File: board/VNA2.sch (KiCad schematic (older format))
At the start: 61 parts, among them U2 LM339, U3 SA612, U4 SA612, U5 SA612, U6 TL082, U7 TL082

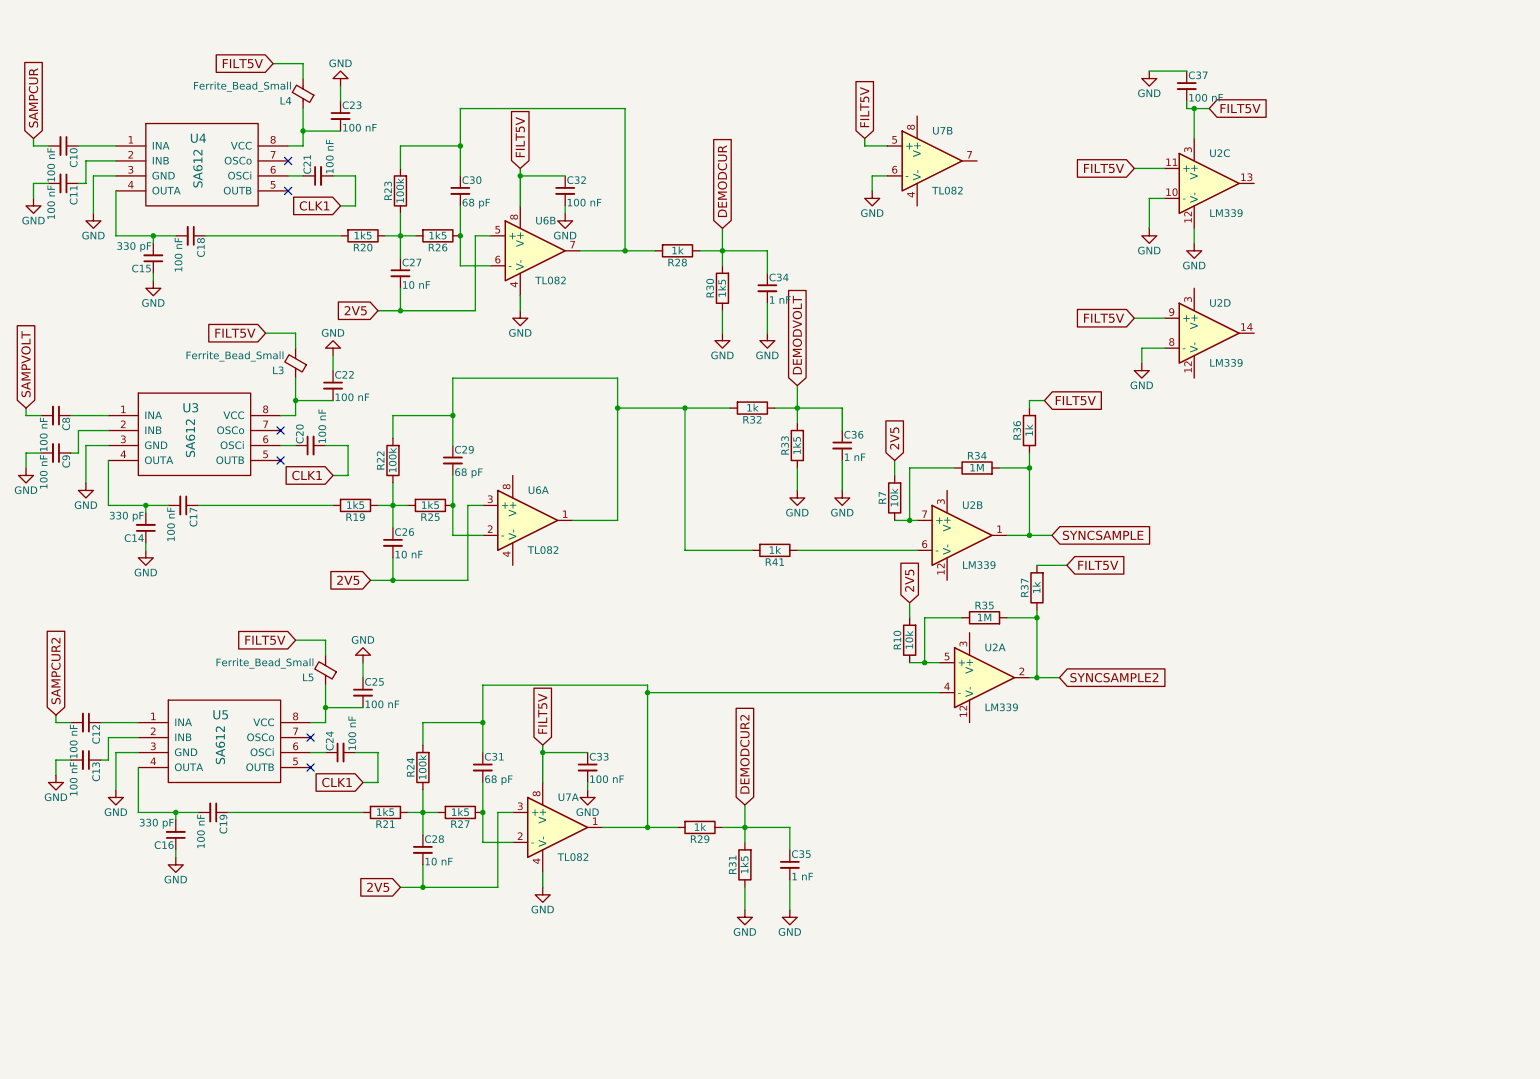
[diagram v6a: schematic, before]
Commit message: Changed TL082 to LM358, other corrections to software
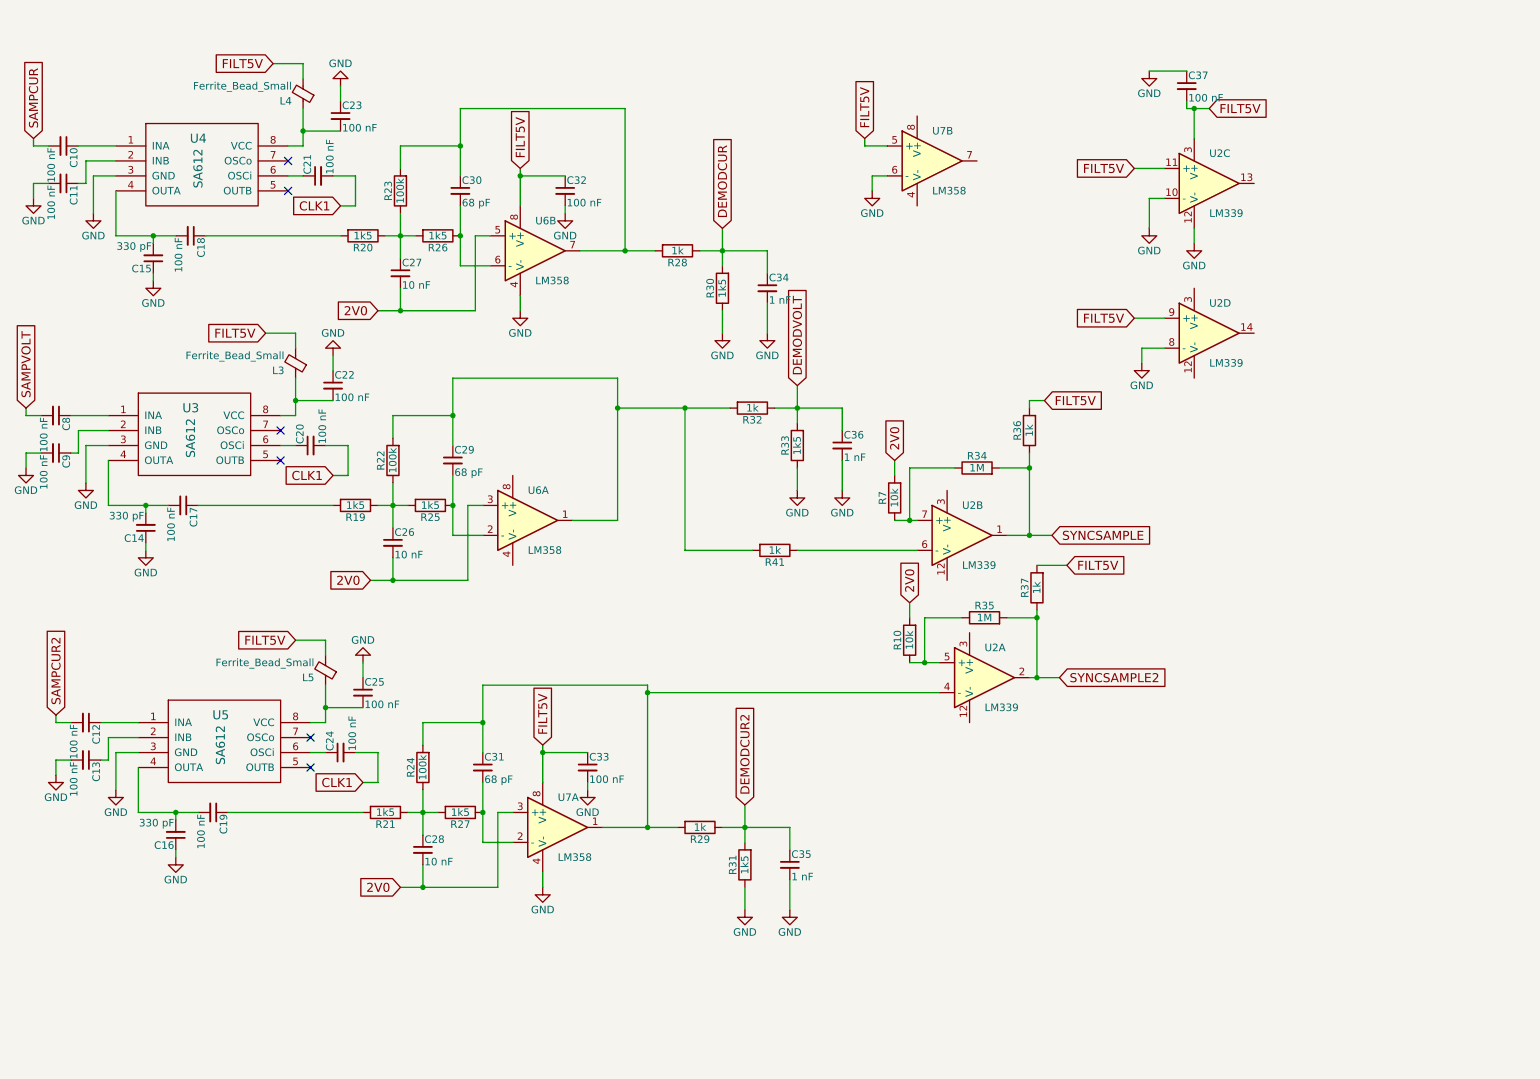
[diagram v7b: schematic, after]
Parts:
- removed U6, U7: TL082, Housings_DIP:DIP-8_W7.62mm_Socket, symbol TL082
- added U6, U7: LM358, Housings_DIP:DIP-8_W7.62mm_Socket, symbol LM358
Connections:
- net FILT5V: now also U6.8 (V+), U7.5 (+), U7.8 (V+)
- net GND: now also U6.4 (V-), U7.4 (V-), U7.6 (-)
- net at C30.2, R26.1: now also U6.6 (-)
- net at C30.1, R23.2, R28.2: now also U6.7
- net at C29.1, R22.2, R32.2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: now also U6.1
- net at C29.2, R25.1: now also U6.2 (-)
- net at C31.1, R24.2, R29.2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: now also U7.1
- net at C31.2, R27.1: now also U7.2 (-)
- net 2V5 renamed 2V0
- net 2V0: now also U6.3 (+), U6.5 (+), U7.3 (+)
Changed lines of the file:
@@
 $EndDescr
-$Comp
-L TL082 U6
-U 2 1 5BB32DA1
-P 4450 2050
-F 0 "U6" H 4450 2250 50  0000 L CNN
-F 1 "TL082" H 4450 1850 50  0000 L CNN
-F 2 "Housings_DIP:DIP-8_W7.62mm_Socket" H 4450 2050 50  0001 C CNN
-F 3 "" H 4450 2050 50  0001 C CNN
-	2    4450 2050
-	1    0    0    -1
-$EndComp
 $Comp
 L SA612 U4
@@
 $EndComp
 Text GLabel 3400 2450 0    60   Input ~ 0
-2V5
+2V0
 $Comp
 L C_Small C27
@@
 $EndComp
 Text GLabel 3350 4250 0    60   Input ~ 0
-2V5
+2V0
 $Comp
 L C_Small C26
@@
 Text GLabel 7900 3950 2    60   Input ~ 0
 SYNCSAMPLE
-$Comp
-L TL082 U7
-U 1 1 5BB496AC
-P 4600 5900
-F 0 "U7" H 4600 6100 50  0000 L CNN
-F 1 "TL082" H 4600 5700 50  0000 L CNN
-F 2 "Housings_DIP:DIP-8_W7.62mm_Socket" H 4600 5900 50  0001 C CNN
-F 3 "" H 4600 5900 50  0001 C CNN
-	1    4600 5900
-	1    0    0    -1
-$EndComp
 $Comp
 L SA612 U5
@@
 $EndComp
 Text GLabel 3550 6300 0    60   Input ~ 0
-2V5
+2V0
 $Comp
 L C_Small C28
@@
 F 3 "" H 6150 6450 50  0001 C CNN
 	1    6150 6450
-	1    0    0    -1
-$EndComp
-$Comp
-L TL082 U7
-U 2 1 5BB4C405
-P 7100 1450
-F 0 "U7" H 7100 1650 50  0000 L CNN
-F 1 "TL082" H 7100 1250 50  0000 L CNN
-F 2 "Housings_DIP:DIP-8_W7.62mm_Socket" H 7100 1450 50  0001 C CNN
-F 3 "" H 7100 1450 50  0001 C CNN
-	2    7100 1450
-	1    0    0    -1
-$EndComp
-$Comp
-L TL082 U6
-U 1 1 5BB32E35
-P 4400 3850
-F 0 "U6" H 4400 4050 50  0000 L CNN
-F 1 "TL082" H 4400 3650 50  0000 L CNN
-F 2 "Housings_DIP:DIP-8_W7.62mm_Socket" H 4400 3850 50  0001 C CNN
-F 3 "" H 4400 3850 50  0001 C CNN
-	1    4400 3850
 	1    0    0    -1
 $EndComp
@@
 $EndComp
 Text GLabel 6850 3450 1    60   Input ~ 0
-2V5
+2V0
 Text GLabel 6950 4400 1    60   Input ~ 0
-2V5
+2V0
 Wire Wire Line
 	6950 3850 6950 3500
@@
 Wire Wire Line
 	5450 4050 5900 4050
+$Comp
+L LM358 U6
+U 1 1 5C1CC28D
+P 4400 3850
+F 0 "U6" H 4400 4050 50  0000 L CNN
+F 1 "LM358" H 4400 3650 50  0000 L CNN
+F 2 "Housings_DIP:DIP-8_W7.62mm_Socket" H 4400 3850 50  0001 C CNN
+F 3 "" H 4400 3850 50  0001 C CNN
+	1    4400 3850
+	1    0    0    -1
+$EndComp
+$Comp
+L LM358 U6
+U 2 1 5C1CC9D0
+P 4450 2050
+F 0 "U6" H 4450 2250 50  0000 L CNN
+F 1 "LM358" H 4450 1850 50  0000 L CNN
+F 2 "Housings_DIP:DIP-8_W7.62mm_Socket" H 4450 2050 50  0001 C CNN
+F 3 "" H 4450 2050 50  0001 C CNN
+	2    4450 2050
+	1    0    0    -1
+$EndComp
+$Comp
+L LM358 U7
+U 1 1 5C1CCB4C
+P 4600 5900
+F 0 "U7" H 4600 6100 50  0000 L CNN
+F 1 "LM358" H 4600 5700 50  0000 L CNN
+F 2 "Housings_DIP:DIP-8_W7.62mm_Socket" H 4600 5900 50  0001 C CNN
+F 3 "" H 4600 5900 50  0001 C CNN
+	1    4600 5900
+	1    0    0    -1
+$EndComp
+$Comp
+L LM358 U7
+U 2 1 5C1CCEA9
+P 7100 1450
+F 0 "U7" H 7100 1650 50  0000 L CNN
+F 1 "LM358" H 7100 1250 50  0000 L CNN
+F 2 "Housings_DIP:DIP-8_W7.62mm_Socket" H 7100 1450 50  0001 C CNN
+F 3 "" H 7100 1450 50  0001 C CNN
+	2    7100 1450
+	1    0    0    -1
+$EndComp
 $EndSCHEMATC
